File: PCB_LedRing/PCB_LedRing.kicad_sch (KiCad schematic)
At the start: 69 parts, among them IC1 PCA9552D,118, J1 Board2Board

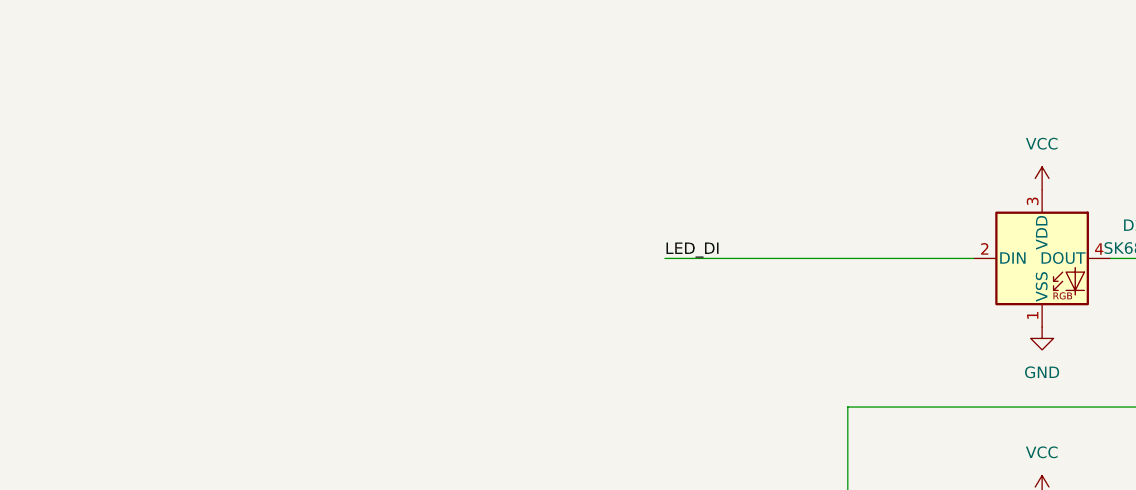
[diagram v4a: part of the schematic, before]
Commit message: Add Level Shifter
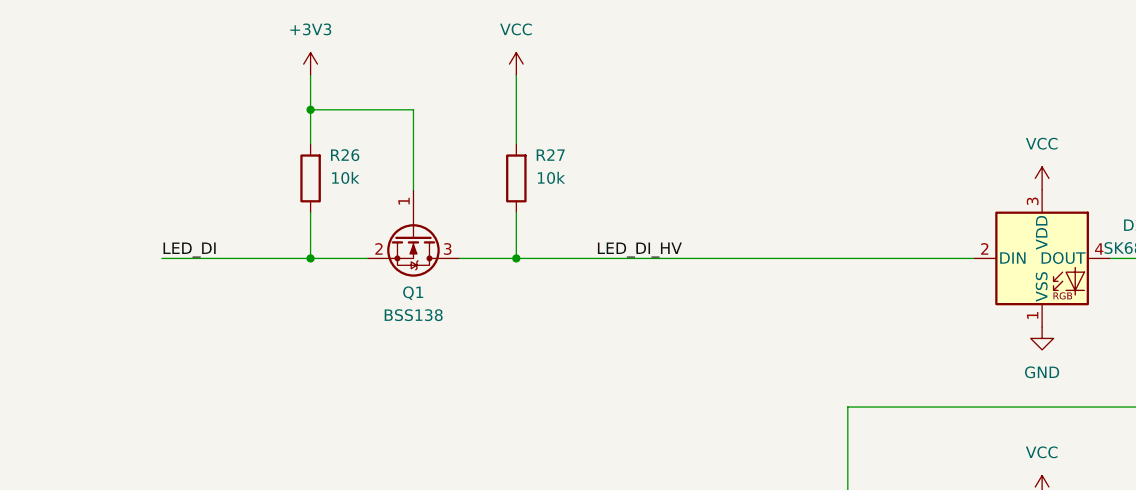
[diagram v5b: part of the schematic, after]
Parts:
- added Q1: BSS138, Package_TO_SOT_SMD:SOT-23, symbol Transistor_FET:BSS138
- added R26, R27: 10k, Resistor_SMD:R_0603_1608Metric_Pad0.98x0.95mm_HandSolder, symbol Device:R
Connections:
- net +3V3: now also Q1.1 (G), R26.2
- net LED_DI: now also Q1.2 (S), R26.1; no longer D2.2 (DIN)
- net VCC: now also R27.2
- new net LED_DI_HV: D2.2 (DIN), Q1.3 (D), R27.1
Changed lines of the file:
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@@
   (title_block
     (title "LED Ring")
-    (date "2024-03-21")
+    (date "2024-03-28")
     (rev "A")
     (company "EberKreis")
@@
   (junction (at 55.88 219.71) (diameter 0) (color 0 0 0 0)
   )
+  (junction (at 139.7 36.83) (diameter 0) (color 0 0 0 0)
+  )
   (junction (at 254 125.73) (diameter 0) (color 0 0 0 0)
   )
@@
   (junction (at 207.01 191.77) (diameter 0) (color 0 0 0 0)
   )
+  (junction (at 139.7 53.34) (diameter 0) (color 0 0 0 0)
+  )
   (junction (at 119.38 259.08) (diameter 0) (color 0 0 0 0)
   )
@@
   (junction (at 322.58 113.03) (diameter 0) (color 0 0 0 0)
   )
+  (junction (at 162.56 53.34) (diameter 0) (color 0 0 0 0)
+  )
   (junction (at 215.9 209.55) (diameter 0) (color 0 0 0 0)
   )
@@
     (stroke (width 0) (type default))
   )
+  (wire (pts (xy 151.13 45.72) (xy 151.13 36.83))
+    (stroke (width 0) (type default))
+  )
   (wire (pts (xy 147.32 217.17) (xy 152.4 217.17))
     (stroke (width 0) (type default))
   )
+  (wire (pts (xy 151.13 36.83) (xy 139.7 36.83))
+    (stroke (width 0) (type default))
+  )
   (wire (pts (xy 199.39 191.77) (xy 207.01 191.77))
     (stroke (width 0) (type default))
@@
     (stroke (width 0) (type default))
   )
+  (wire (pts (xy 139.7 36.83) (xy 139.7 40.64))
+    (stroke (width 0) (type default))
+  )
   (wire (pts (xy 55.88 207.01) (xy 55.88 209.55))
     (stroke (width 0) (type default))
@@
     (stroke (width 0) (type default))
   )
+  (wire (pts (xy 156.21 53.34) (xy 162.56 53.34))
+    (stroke (width 0) (type default))
+  )
   (wire (pts (xy 182.88 204.47) (xy 199.39 204.47))
     (stroke (width 0) (type default))
@@
     (stroke (width 0) (type default))
   )
+  (wire (pts (xy 139.7 33.02) (xy 139.7 36.83))
+    (stroke (width 0) (type default))
+  )
   (wire (pts (xy 44.45 229.87) (xy 44.45 232.41))
     (stroke (width 0) (type default))
@@
     (stroke (width 0) (type default))
   )
+  (wire (pts (xy 162.56 53.34) (xy 162.56 48.26))
+    (stroke (width 0) (type default))
+  )
   (wire (pts (xy 223.52 257.81) (xy 214.63 257.81))
     (stroke (width 0) (type default))
@@
     (stroke (width 0) (type default))
   )
+  (wire (pts (xy 139.7 53.34) (xy 146.05 53.34))
+    (stroke (width 0) (type default))
+  )
+  (wire (pts (xy 139.7 48.26) (xy 139.7 53.34))
+    (stroke (width 0) (type default))
+  )
   (wire (pts (xy 182.88 222.25) (xy 189.23 222.25))
     (stroke (width 0) (type default))
@@
     (stroke (width 0) (type default))
   )
+  (wire (pts (xy 162.56 33.02) (xy 162.56 40.64))
+    (stroke (width 0) (type default))
+  )
   (wire (pts (xy 46.99 57.15) (xy 52.07 57.15))
     (stroke (width 0) (type default))
@@
     (stroke (width 0) (type default))
   )
+  (wire (pts (xy 123.19 53.34) (xy 139.7 53.34))
+    (stroke (width 0) (type default))
+  )
   (wire (pts (xy 134.62 212.09) (xy 139.7 212.09))
     (stroke (width 0) (type default))
@@
     (stroke (width 0) (type default))
   )
-  (wire (pts (xy 179.07 53.34) (xy 213.36 53.34))
+  (wire (pts (xy 162.56 53.34) (xy 213.36 53.34))
     (stroke (width 0) (type default))
   )
@@
     (effects (font (size 1.27 1.27)) (justify left bottom))
   )
+  (label "LED_DI_HV" (at 171.45 53.34 0) (fields_autoplaced)
+    (effects (font (size 1.27 1.27)) (justify left bottom))
+  )
   (label "2D" (at 134.62 224.79 0) (fields_autoplaced)
     (effects (font (size 1.27 1.27)) (justify left bottom))
@@
     (effects (font (size 1.27 1.27)) (justify right bottom))
   )
-  (label "LED_DI" (at 179.07 53.34 0) (fields_autoplaced)
+  (label "LED_DI" (at 123.19 53.34 0) (fields_autoplaced)
     (effects (font (size 1.27 1.27)) (justify left bottom))
   )
@@
     )
   )
+  (symbol (lib_id "power:+3V3") (at 139.7 33.02 0) (unit 1)
+    (in_bom yes) (on_board yes) (dnp no) (fields_autoplaced)
+    (property "Reference" "#PWR054" (at 139.7 36.83 0)
+      (effects (font (size 1.27 1.27)) hide)
+    )
+    (property "Value" "+3V3" (at 139.7 27.94 0)
+      (effects (font (size 1.27 1.27)))
+    )
+    (property "Footprint" "" (at 139.7 33.02 0)
+      (effects (font (size 1.27 1.27)) hide)
+    )
+    (property "Datasheet" "" (at 139.7 33.02 0)
+      (effects (font (size 1.27 1.27)) hide)
+    )
+    (pin "1")
+    (instances
+      (project "PCB_LedRing"
+        (path "/8b82cf3e-088b-415c-b4d2-cbd128176492"
+          (reference "#PWR054") (unit 1)
+        )
+      )
+    )
+  )
   (symbol (lib_id "power:GND") (at 31.75 232.41 0) (unit 1)
     (in_bom yes) (on_board yes) (dnp no) (fields_autoplaced)
@@
     )
   )
+  (symbol (lib_id "power:VCC") (at 162.56 33.02 0) (unit 1)
+    (in_bom yes) (on_board yes) (dnp no) (fields_autoplaced)
+    (property "Reference" "#PWR034" (at 162.56 36.83 0)
+      (effects (font (size 1.27 1.27)) hide)
+    )
+    (property "Value" "VCC" (at 162.56 27.94 0)
+      (effects (font (size 1.27 1.27)))
+    )
+    (property "Footprint" "" (at 162.56 33.02 0)
+      (effects (font (size 1.27 1.27)) hide)
+    )
+    (property "Datasheet" "" (at 162.56 33.02 0)
+      (effects (font (size 1.27 1.27)) hide)
+    )
+    (pin "1")
+    (instances
+      (project "PCB_LedRing"
+        (path "/8b82cf3e-088b-415c-b4d2-cbd128176492"
+          (reference "#PWR034") (unit 1)
+        )
+      )
+    )
+  )
   (symbol (lib_id "power:VCC") (at 67.31 50.8 0) (unit 1)
     (in_bom yes) (on_board yes) (dnp no) (fields_autoplaced)
@@
     )
   )
+  (symbol (lib_id "Device:R") (at 162.56 44.45 180) (unit 1)
+    (in_bom yes) (on_board yes) (dnp no)
+    (property "Reference" "R27" (at 166.37 41.91 0)
+      (effects (font (size 1.27 1.27)))
+    )
+    (property "Value" "10k" (at 166.37 44.45 0)
+      (effects (font (size 1.27 1.27)))
+    )
+    (property "Footprint" "Resistor_SMD:R_0603_1608Metric_Pad0.98x0.95mm_HandSolder" (at 164.338 44.45 90)
+      (effects (font (size 1.27 1.27)) hide)
+    )
+    (property "Datasheet" "~" (at 162.56 44.45 0)
+      (effects (font (size 1.27 1.27)) hide)
+    )
+    (pin "2")
+    (pin "1")
+    (instances
+      (project "PCB_LedRing"
+        (path "/8b82cf3e-088b-415c-b4d2-cbd128176492"
+          (reference "R27") (unit 1)
+        )
+      )
+    )
+  )
   (symbol (lib_id "power:GND") (at 49.53 64.77 0) (mirror y) (unit 1)
     (in_bom yes) (on_board yes) (dnp no) (fields_autoplaced)
@@
     )
   )
+  (symbol (lib_id "Device:R") (at 139.7 44.45 180) (unit 1)
+    (in_bom yes) (on_board yes) (dnp no)
+    (property "Reference" "R26" (at 143.51 41.91 0)
+      (effects (font (size 1.27 1.27)))
+    )
+    (property "Value" "10k" (at 143.51 44.45 0)
+      (effects (font (size 1.27 1.27)))
+    )
+    (property "Footprint" "Resistor_SMD:R_0603_1608Metric_Pad0.98x0.95mm_HandSolder" (at 141.478 44.45 90)
+      (effects (font (size 1.27 1.27)) hide)
+    )
+    (property "Datasheet" "~" (at 139.7 44.45 0)
+      (effects (font (size 1.27 1.27)) hide)
+    )
+    (pin "2")
+    (pin "1")
+    (instances
+      (project "PCB_LedRing"
+        (path "/8b82cf3e-088b-415c-b4d2-cbd128176492"
+          (reference "R26") (unit 1)
+        )
+      )
+    )
+  )
   (symbol (lib_id "Device:C") (at 231.14 262.89 0) (unit 1)
     (in_bom yes) (on_board yes) (dnp no)
@@
         )
       )
+    )
+  )
+  (symbol (lib_id "Transistor_FET:BSS138") (at 151.13 50.8 270) (unit 1)
+    (in_bom yes) (on_board yes) (dnp no) (fields_autoplaced)
+    (property "Reference" "Q1" (at 151.13 57.15 90)
+      (effects (font (size 1.27 1.27)))
+    )
+    (property "Value" "BSS138" (at 151.13 59.69 90)
+      (effects (font (size 1.27 1.27)))
+    )
+    (property "Footprint" "Package_TO_SOT_SMD:SOT-23" (at 149.225 55.88 0)
+      (effects (font (size 1.27 1.27) italic) (justify left) hide)
+    )
+    (property "Datasheet" "https://www.onsemi.com/pub/Collateral/BSS138-D.PDF" (at 147.32 55.88 0)
+      (effects (font (size 1.27 1.27)) (justify left) hide)
+    )
+    (pin "1")
+    (pin "2")
+    (pin "3")
+    (instances
+      (project "PCB_LedRing"
+        (path "/8b82cf3e-088b-415c-b4d2-cbd128176492"
+          (reference "Q1") (unit 1)
+        )
+      )

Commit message: Add Mouser numbers
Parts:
- J1: Mouser (none) -> 649-1012938390602BLF
- Q1: Mouser (none) -> 512-BSS138
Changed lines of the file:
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@@
+      (effects (font (size 1.27 1.27)) hide)
+    )
+    (property "Mouser" "649-1012938390602BLF" (at 57.15 57.15 0)
       (effects (font (size 1.27 1.27)) hide)
     )
@@
       (effects (font (size 1.27 1.27) italic) hide)
     )
-    (property "Datasheet" "LDS-SMHTA5604RISIT" (at 121.92 212.09 0)
+    (property "Datasheet" "https://www.mouser.ch/datasheet/2/244/LUMXS09495_1-2551559.pdf" (at 121.92 212.09 0)
       (effects (font (size 1.27 1.27) italic) hide)
     )
@@
       (effects (font (size 1.27 1.27) italic) hide)
     )
-    (property "Datasheet" "LDS-SMHTA5604RISIT" (at 217.17 232.41 0)
+    (property "Datasheet" "https://www.mouser.ch/datasheet/2/244/LUMXS09495_1-2551559.pdf" (at 217.17 232.41 0)
       (effects (font (size 1.27 1.27) italic) hide)
     )
@@
       (effects (font (size 1.27 1.27)) (justify left) hide)
     )
-    (pin "1")
+    (property "Mouser" "512-BSS138" (at 151.13 50.8 90)
+      (effects (font (size 1.27 1.27)) hide)
+    )
+    (pin "1")
